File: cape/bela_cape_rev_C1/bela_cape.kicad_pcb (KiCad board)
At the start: 4 copper layers, 71.8 x 54.6 mm, 141 parts, among them IC1 PAM8406, IC2 TLV320AIC3104, IC3 MIC5317, IC4 TL974, IC5 TL974, IC6 ES9080Q, IC7 TSV524xIQ4T, IC8 TSV524xIQ4T, IC9 ADS8168, J1 Conn_01x02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

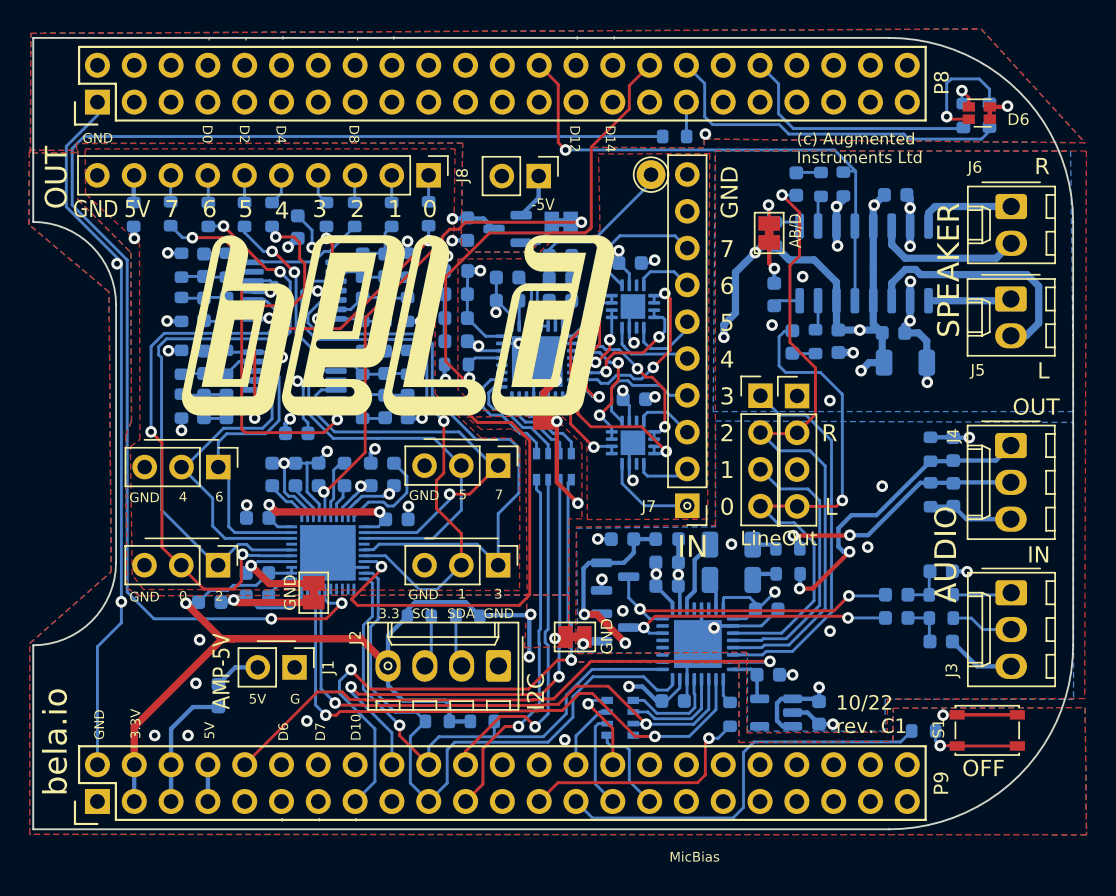
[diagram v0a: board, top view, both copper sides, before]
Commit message: First complete iteration of C1 cape layout
(cherry picked from commit 0ee733c70b42f416809330055e007cefcdb105fa)
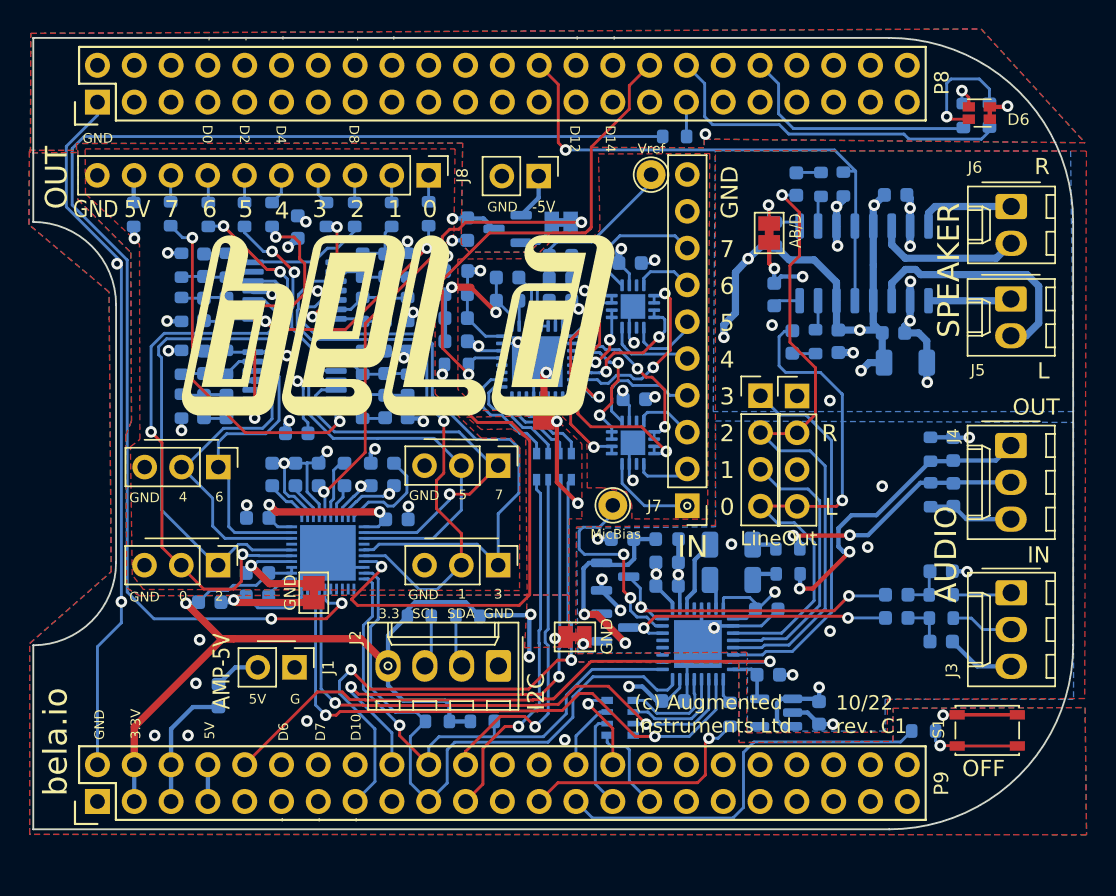
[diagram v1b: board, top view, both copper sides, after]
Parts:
- added TP2: TestPoint, TestPoint:TestPoint_THTPad_D2.0mm_Drill1.0mm, F.Cu at (152.6, 110.0)
- C21, C22, C26, C27, C30, C31, C35, C36: value C -> 220pF
- R11, R13, R15, R17, R19, R21, R23, R25: value R -> 22k/0.5%
- R12, R14, R16, R18, R20, R22, R24, R26: value R -> 16.9k/0.5%
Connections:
- IC2 pad 15: unconnected-(IC2-Pad15) -> /Audio Codec/MICBIAS
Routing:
- net GNDA: track 129.4 -> 144.1 mm, vias 49 -> 51
- net /Audio Codec/MICBIAS: track 0.00 -> 14.6 mm, vias 0 -> 2
- net +5V_AMP: track 101.6 -> 98.6 mm, vias 6 -> 5
- net Net-(IC8-Pad15): track 10.9 -> 13.2 mm
- net /Analog Output/ANALOG_OUT3: track 11.7 -> 12.8 mm
- net /Analog Output/ANALOG_OUT7: track 29.2 -> 28.3 mm
- net /Analog Output/DAC3: track 41.9 -> 42.6 mm
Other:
- board text added: "+"
- board text added: "Vref"
